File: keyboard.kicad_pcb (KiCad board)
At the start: 4 copper layers, 17.8 x 33 mm, 20 parts, among them J1 Conn_01x12, J2 Conn_01x12, U1 ATmega32U4-MU, U2 ATmega32U4-AU, Y1 Crystal_GND24_Small

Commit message: added ground vias to link the seperate ground planes
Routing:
- net GND: vias 6 -> 8

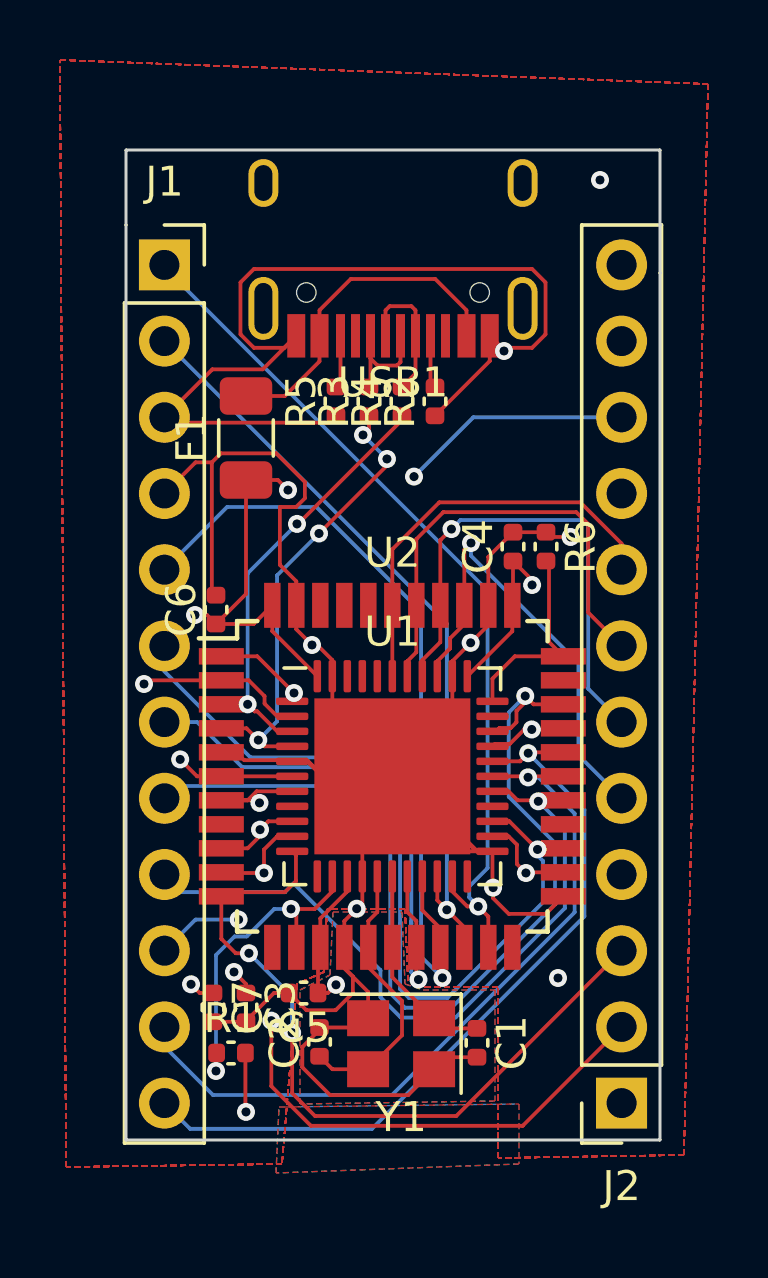
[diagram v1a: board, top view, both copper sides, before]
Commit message: fixed zone issues
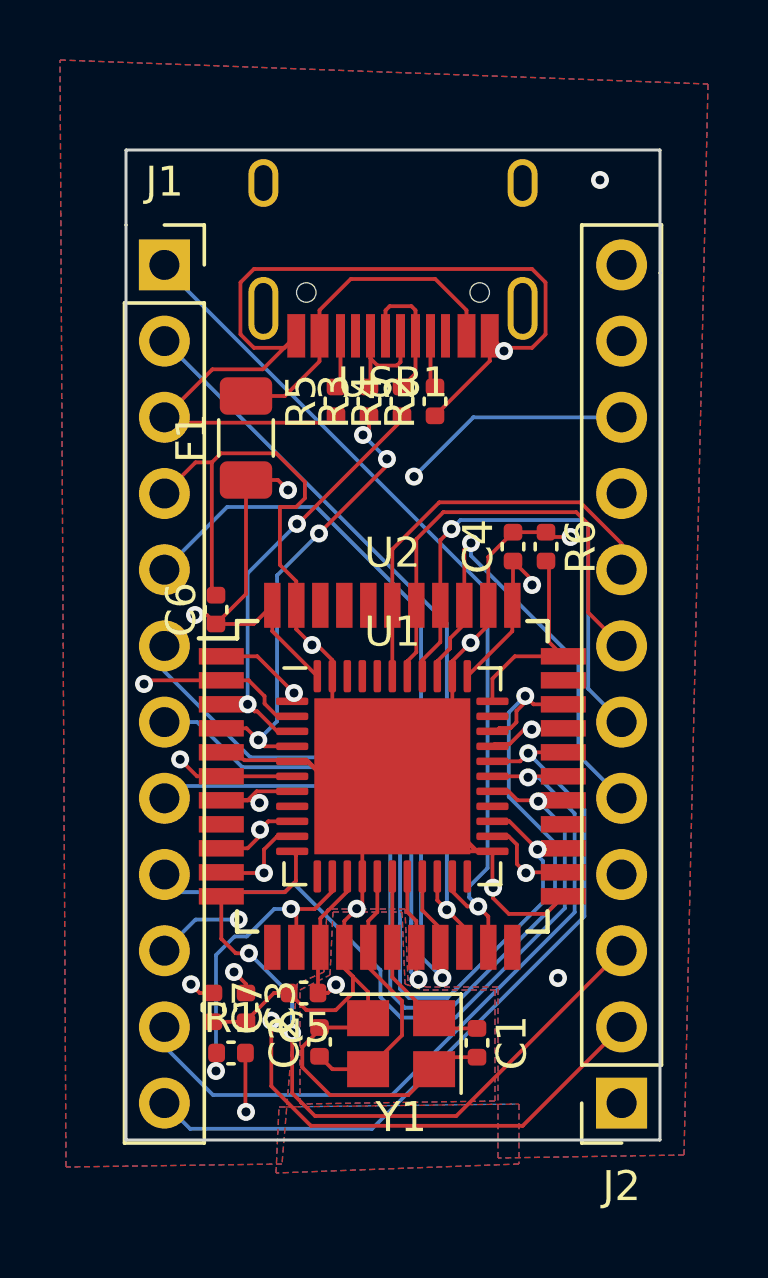
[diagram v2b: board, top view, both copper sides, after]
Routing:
- removed copper zone on F.Cu, net (none)
- removed copper zone on Ground, net (none)
